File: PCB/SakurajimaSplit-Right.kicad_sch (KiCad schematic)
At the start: 46 parts, among them J15 SWD, J16 Conn_01x01_Pin, J17 Conn_01x01_Pin, J18 Conn_01x01_Pin, J20 Conn_01x01_Pin, J21 Conn_01x01_Pin, J22 Conn_01x01_Pin, J23 Conn_01x01_Pin, J24 Conn_01x01_Pin, J25 Conn_01x01_Pin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

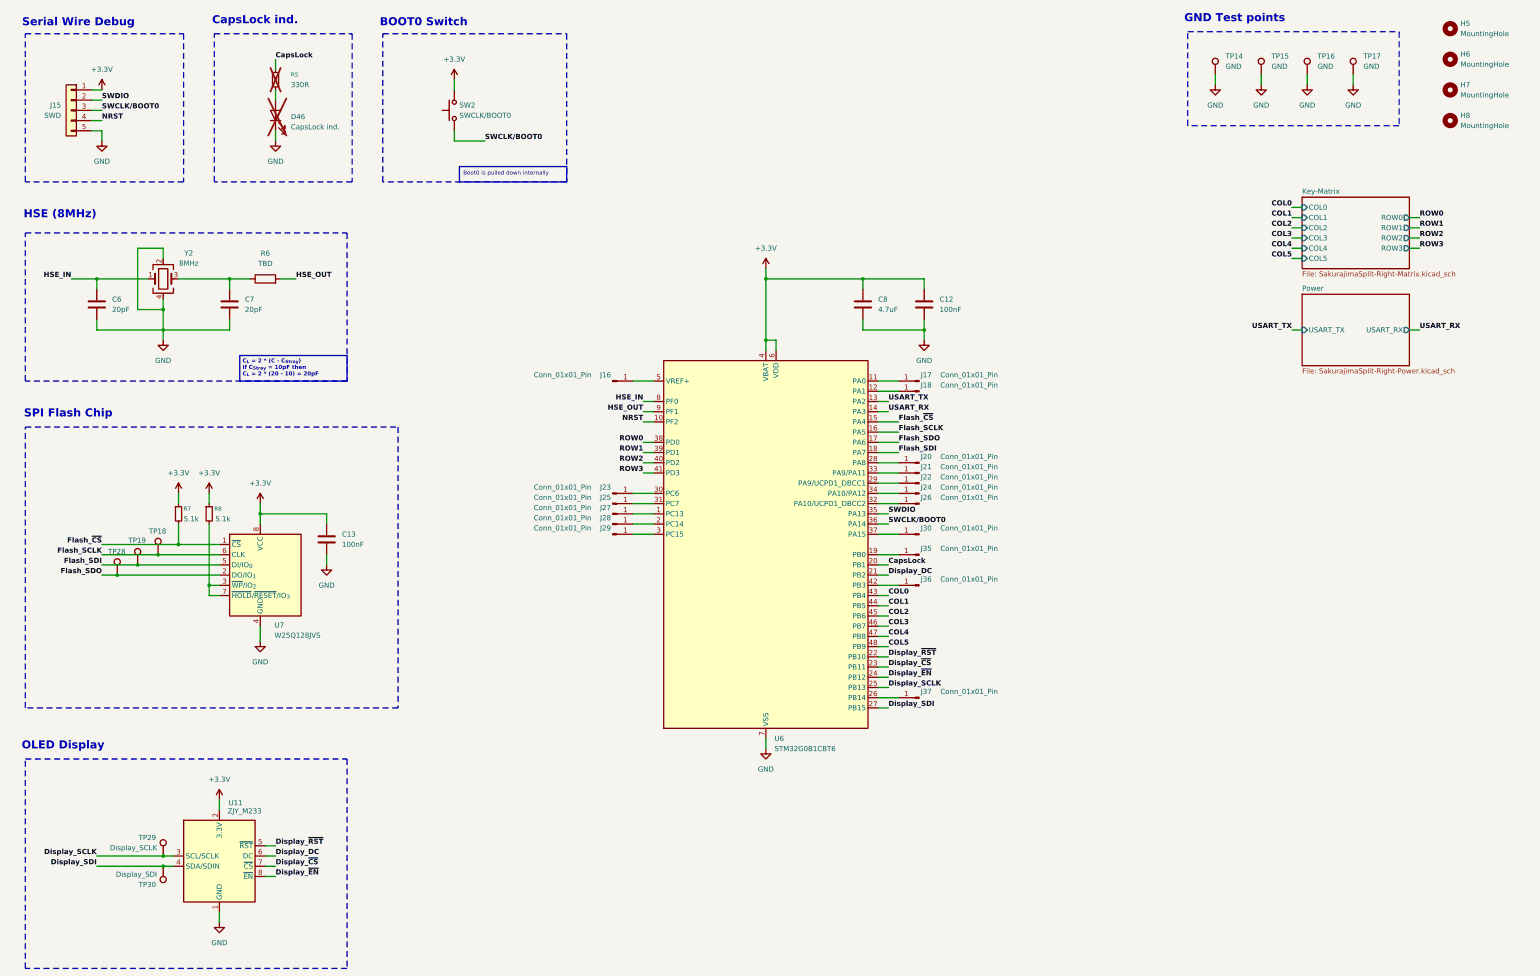
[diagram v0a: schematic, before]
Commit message: feat(pcb): finish designing rough layout and update schematic
- Removed unused MCU pads
- Removed some GND testpoints
- Updated MCU connections based on PCB layout and MCU orientation
- Updated key matrix layout for a less aggressive one which feels more
  comfortable and more visually pleasing
- Re-annotated schematic
- Finished rough component placement
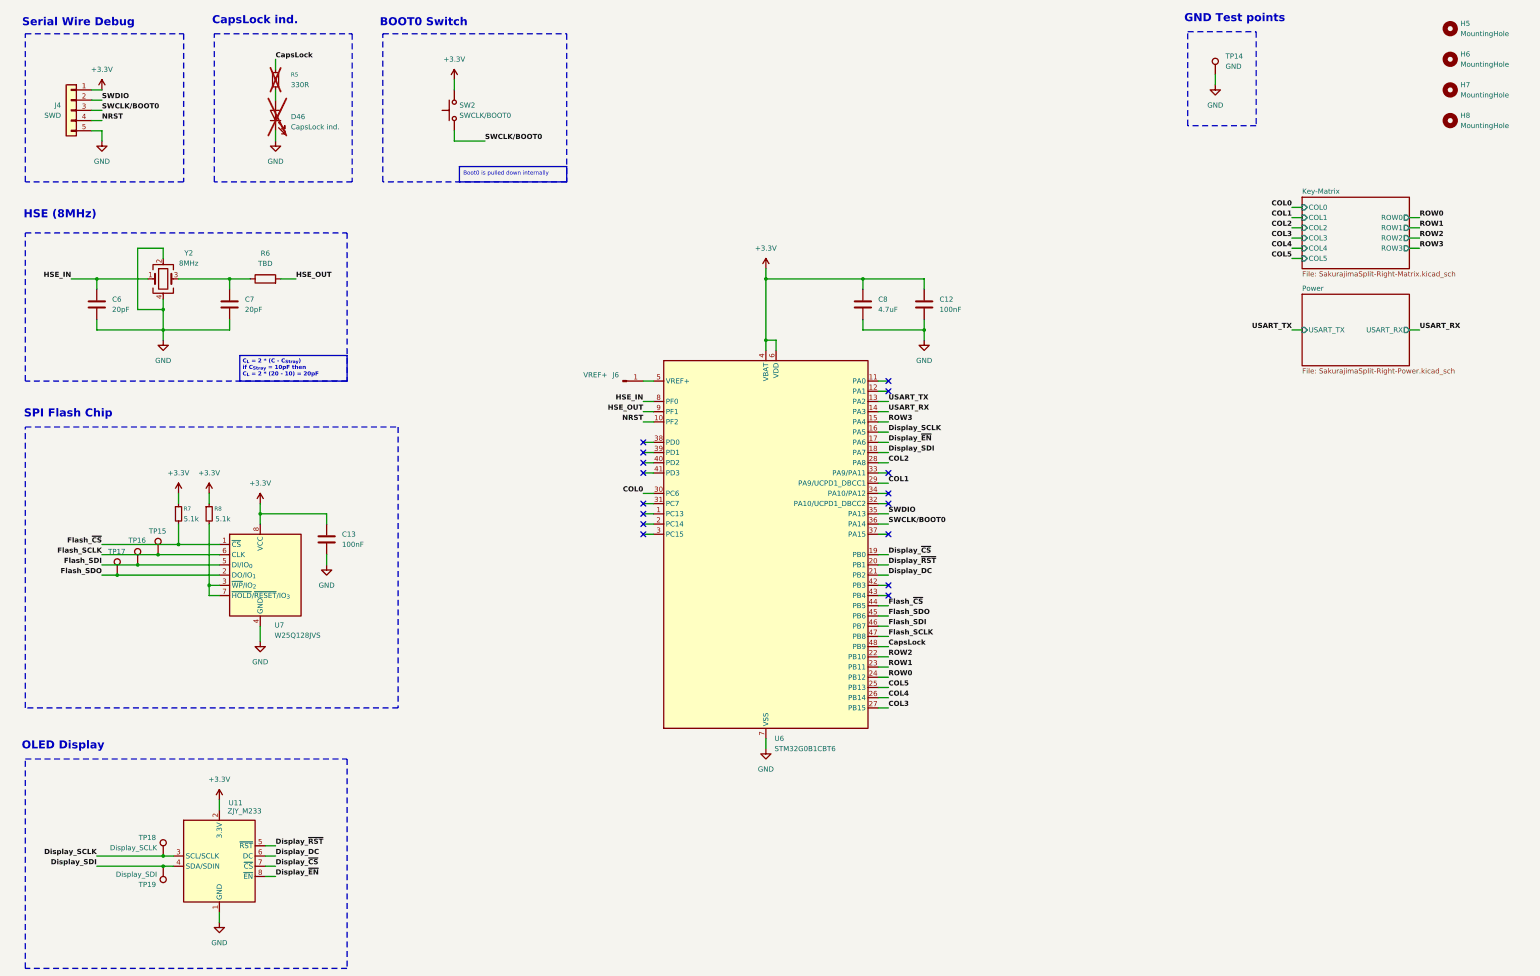
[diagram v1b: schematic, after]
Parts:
- removed J16, J17, J18, J20, J21, J22, J23, J24, J25, J26, J27, J28, J29, J30, J35, J36, J37: Conn_01x01_Pin, Connector_Wire:SolderWirePad_1x01_SMD_1x2mm, symbol Connector:Conn_01x01_Pin
- removed TP15, TP16, TP17: GND, Hayata_Lib:TestPoint_Pad_Circular_1.3mm, symbol Connector:TestPoint
- added J6: VREF+, Connector_Wire:SolderWirePad_1x01_SMD_1x2mm, symbol Connector:Conn_01x01_Pin
- renumbered J15 to J4, TP18 to TP15, TP19 to TP16, TP28 to TP17, TP29 to TP18, TP30 to TP19
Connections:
- net COL0: now also U6.30 (PC6); no longer U6.43 (PB4)
- net COL1: now also U6.29 (PA9/UCPD1_DBCC1); no longer U6.44 (PB5)
- net COL2: now also U6.28 (PA8); no longer U6.45 (PB6)
- net COL3: now also U6.27 (PB15); no longer U6.46 (PB7)
- net COL4: now also U6.26 (PB14); no longer U6.47 (PB8)
- net COL5: now also U6.25 (PB13); no longer U6.48 (PB9)
- net CapsLock: now also U6.48 (PB9); no longer U6.20 (PB1)
- net Display_SCLK: now also U6.16 (PA5); no longer U6.25 (PB13)
- net Display_SDI: now also U6.18 (PA7); no longer U6.27 (PB15)
- net Display_~{CS}: now also U6.19 (PB0); no longer U6.23 (PB11)
- net Display_~{EN}: now also U6.17 (PA6); no longer U6.24 (PB12)
- net Display_~{RST}: now also U6.20 (PB1); no longer U6.22 (PB10)
- net Flash_SCLK: now also U6.47 (PB8); no longer U6.16 (PA5)
- net Flash_SDI: now also U6.46 (PB7); no longer U6.18 (PA7)
- net Flash_SDO: now also U6.45 (PB6); no longer U6.17 (PA6)
- net Flash_~{CS}: now also U6.44 (PB5); no longer U6.15 (PA4)
- net ROW0: now also U6.24 (PB12); no longer U6.38 (PD0)
- net ROW1: now also U6.23 (PB11); no longer U6.39 (PD1)
- net ROW2: now also U6.22 (PB10); no longer U6.40 (PD2)
- net ROW3: now also U6.15 (PA4); no longer U6.41 (PD3)
- net at U6.5 (VREF+): now also J6.1 (Pin_1)
- no-connect marks 0 -> 16

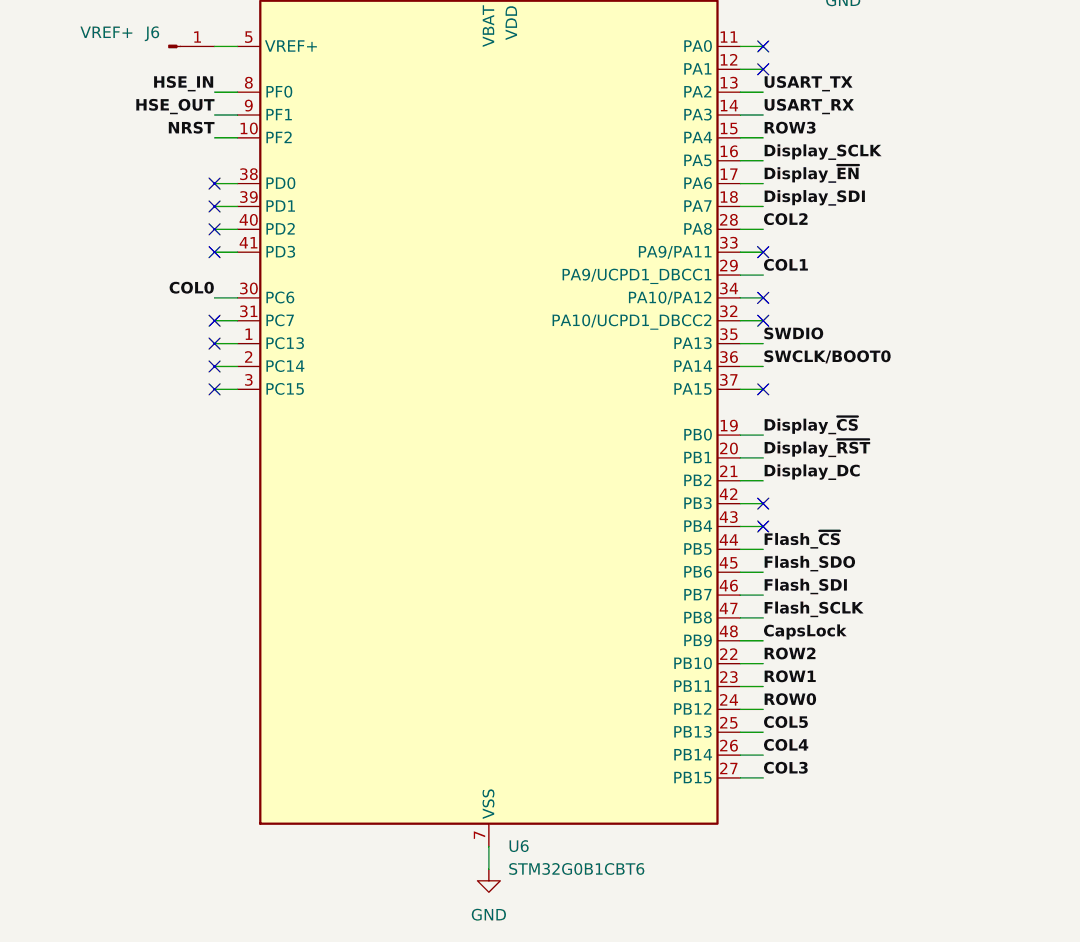
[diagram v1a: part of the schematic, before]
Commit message: feat(pcb): route right half
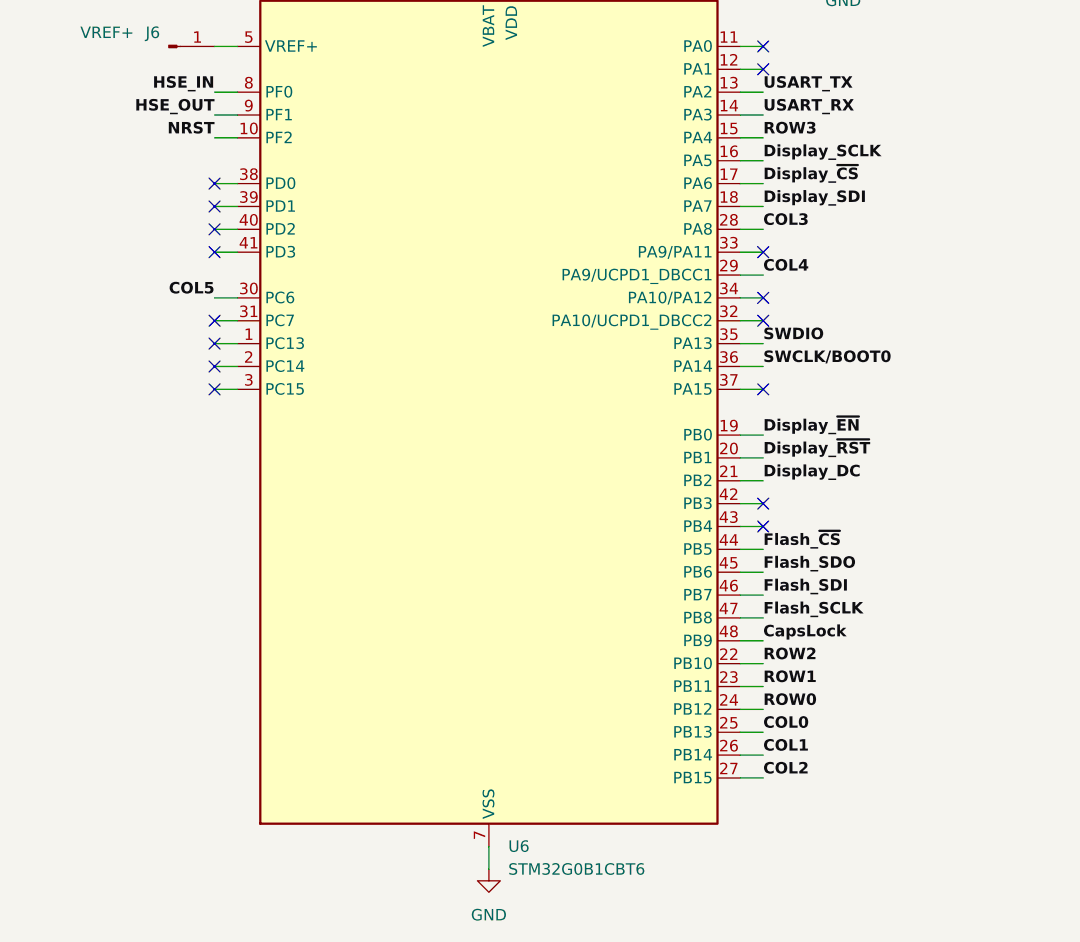
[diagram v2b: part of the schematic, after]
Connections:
- net COL0: now also U6.25 (PB13); no longer U6.30 (PC6)
- net COL1: now also U6.26 (PB14); no longer U6.29 (PA9/UCPD1_DBCC1)
- net COL2: now also U6.27 (PB15); no longer U6.28 (PA8)
- net COL3: now also U6.28 (PA8); no longer U6.27 (PB15)
- net COL4: now also U6.29 (PA9/UCPD1_DBCC1); no longer U6.26 (PB14)
- net COL5: now also U6.30 (PC6); no longer U6.25 (PB13)
- net Display_~{CS}: now also U6.17 (PA6); no longer U6.19 (PB0)
- net Display_~{EN}: now also U6.19 (PB0); no longer U6.17 (PA6)
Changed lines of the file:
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@@
 	)
 	(label "Display_~{EN}"
-		(at 240.03 129.54 0)
+		(at 240.03 157.48 0)
 		(effects
 			(font
@@
 	)
 	(label "COL3"
-		(at 240.03 195.58 0)
+		(at 240.03 134.62 0)
 		(effects
 			(font
@@
 	)
 	(label "COL4"
-		(at 240.03 193.04 0)
+		(at 240.03 139.7 0)
 		(effects
 			(font
@@
 	)
 	(label "COL0"
-		(at 179.07 142.24 180)
-		(effects
-			(font
-				(size 1.27 1.27)
-				(thickness 0.254)
-				(bold yes)
-			)
-			(justify right bottom)
+		(at 240.03 190.5 0)
+		(effects
+			(font
+				(size 1.27 1.27)
+				(thickness 0.254)
+				(bold yes)
+			)
+			(justify left bottom)
 		)
 	)
@@
 	)
 	(label "COL1"
-		(at 240.03 139.7 0)
+		(at 240.03 193.04 0)
 		(effects
 			(font
@@
 	)
 	(label "Display_~{CS}"
-		(at 240.03 157.48 0)
+		(at 240.03 129.54 0)
 		(effects
 			(font
@@
 	)
 	(label "COL2"
-		(at 240.03 134.62 0)
+		(at 240.03 195.58 0)
 		(effects
 			(font
@@
 	)
 	(label "COL5"
-		(at 240.03 190.5 0)
-		(effects
-			(font
-				(size 1.27 1.27)
-				(thickness 0.254)
-				(bold yes)
-			)
-			(justify left bottom)
-		)
-	)
+		(at 179.07 142.24 180)
+		(effects
+			(font
+				(size 1.27 1.27)
+				(thickness 0.254)
+				(bold yes)
+			)
+			(justify right bottom)
+		)
+	)

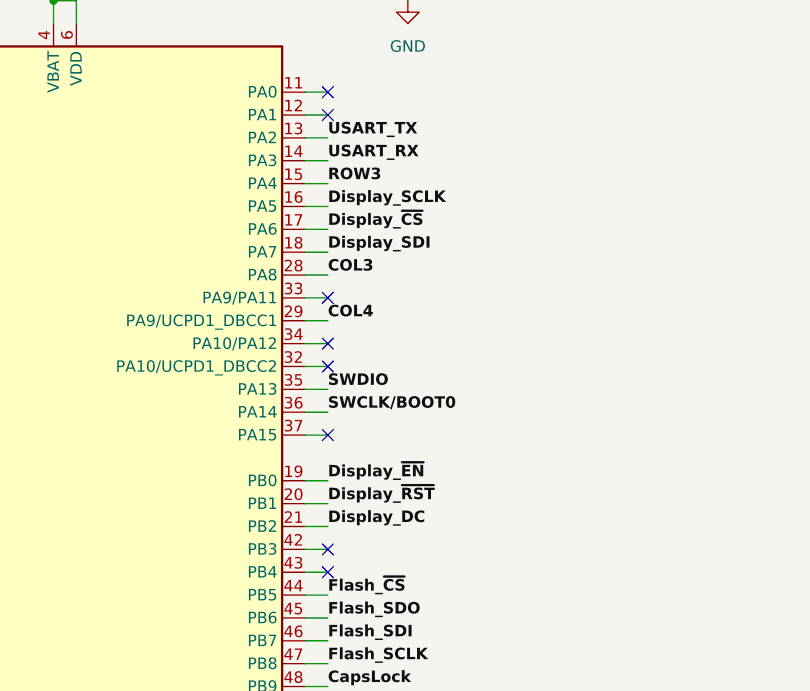
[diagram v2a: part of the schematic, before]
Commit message: fix(pcb): fix DRC errors, fix silkscreen, fix some routing
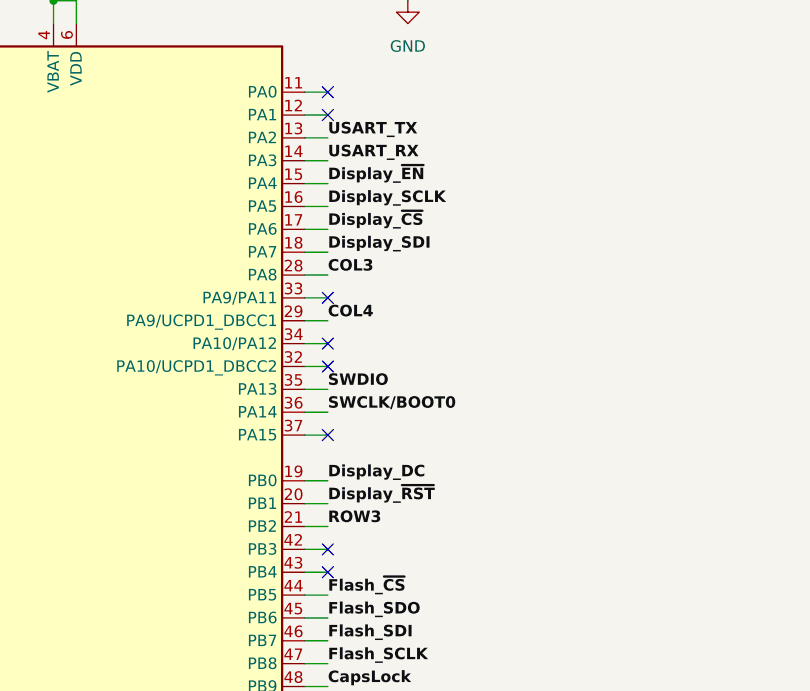
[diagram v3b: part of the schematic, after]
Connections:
- net Display_DC: now also U6.19 (PB0); no longer U6.21 (PB2)
- net Display_~{EN}: now also U6.15 (PA4); no longer U6.19 (PB0)
- net ROW3: now also U6.21 (PB2); no longer U6.15 (PA4)
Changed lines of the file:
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@@
 	)
 	(label "Display_~{EN}"
-		(at 240.03 157.48 0)
+		(at 240.03 124.46 0)
 		(effects
 			(font
@@
 	)
 	(label "ROW3"
-		(at 240.03 124.46 0)
+		(at 240.03 162.56 0)
 		(effects
 			(font
@@
 	)
 	(label "Display_DC"
-		(at 240.03 162.56 0)
-		(effects
-			(font
+		(at 240.03 157.48 0)
+		(effects
+			(font

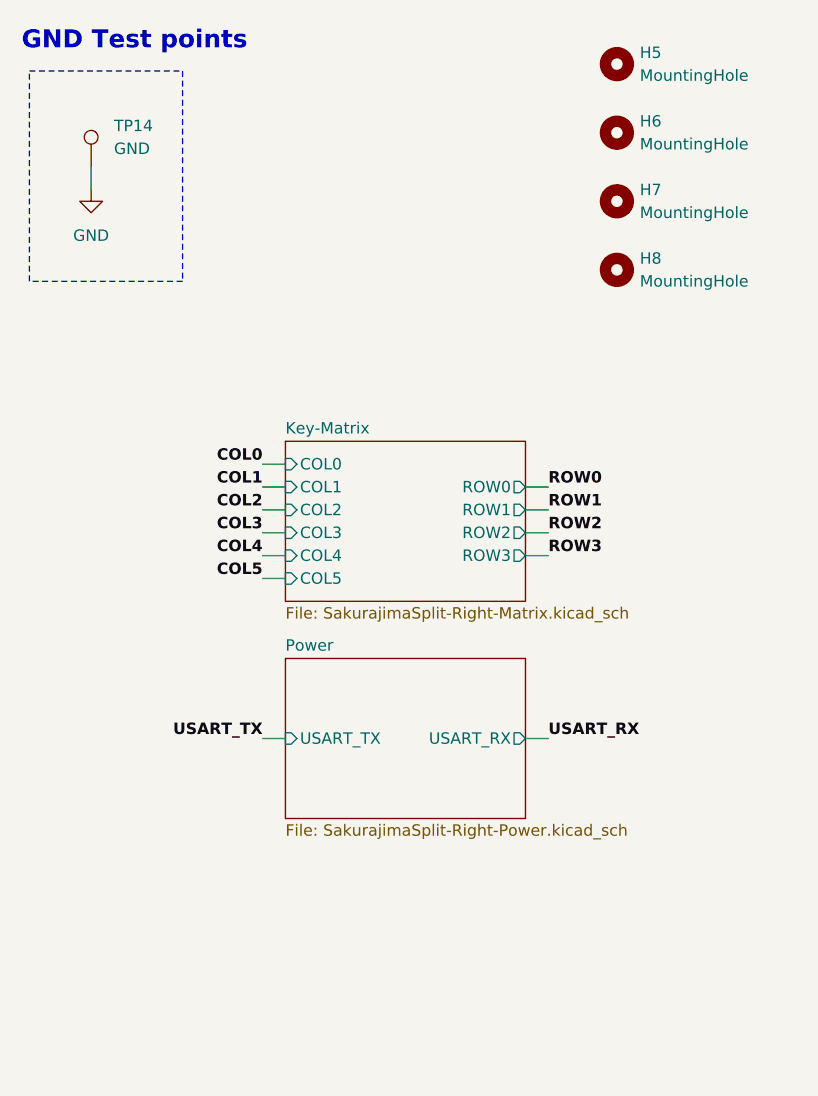
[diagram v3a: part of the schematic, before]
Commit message: feat(pcb): add mounting holes, fix some bugs
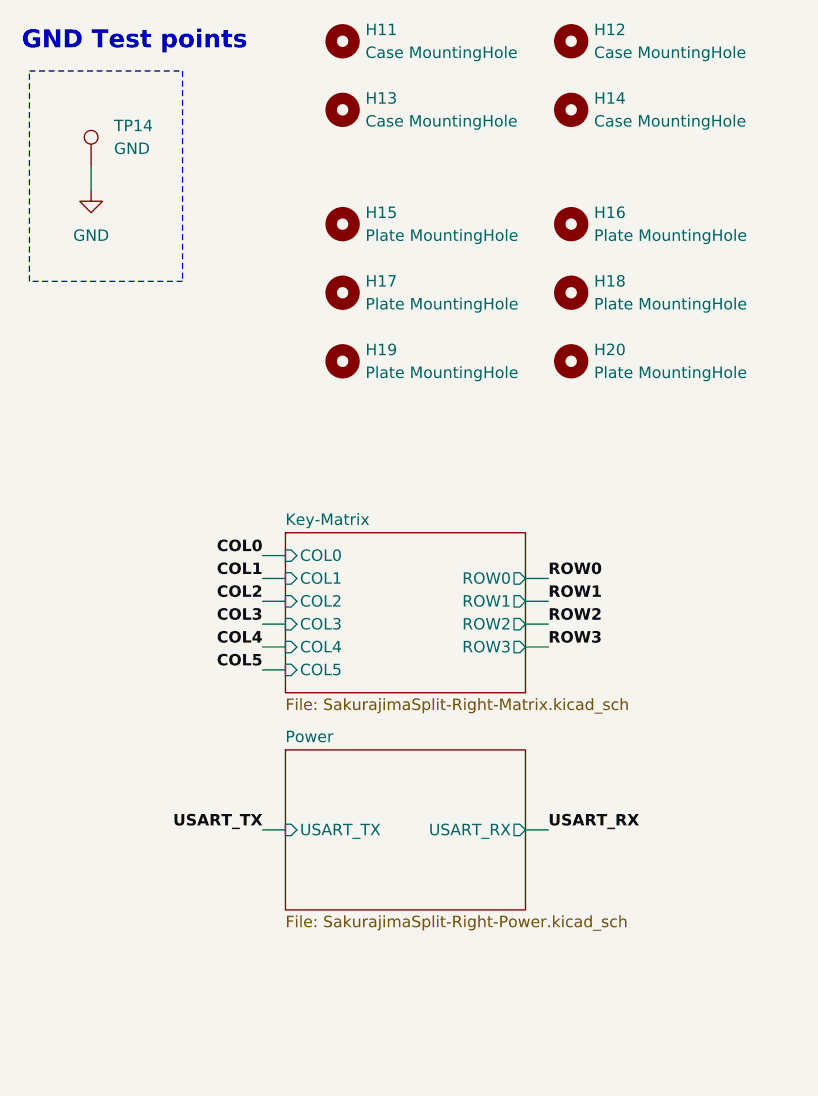
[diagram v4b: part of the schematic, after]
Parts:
- removed H5, H6, H7, H8: MountingHole, MountingHole:MountingHole_3.2mm_M3_Pad_Via, symbol Mechanical:MountingHole
- added H11, H12, H13, H14: Case MountingHole, MountingHole:MountingHole_3.2mm_M3_Pad_Via, symbol Mechanical:MountingHole
- added H15, H16, H17, H18, H19, H20: Plate MountingHole, MountingHole:MountingHole_2.2mm_M2_Pad_Via, symbol Mechanical:MountingHole
- C13: Distributor Link (none) -> https://lionelectronic.ir/products/4734-GRM188R72A104KA35D; Manufacturer (none) -> Murata; Manufacturer Part No. (none) -> GRM188R72A104KA35D
- SW2: Distributor Link https://lionelectronic.ir/products/5092-TS-1187A-B-A-B -> https://lionelectronic.ir/products/5480-TS-1010B-B-A; Manufacturer Part No. TS-1187A-B-A-B -> TS-1010B-B-A
